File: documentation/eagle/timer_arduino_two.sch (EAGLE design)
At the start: 25 parts, among them J1 SMA420564 LED module, Q1 16 Mhz, U1 328P, U2 LM317

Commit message: Version 1.0
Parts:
- removed J1: SMA420564 LED module, SparkFun-Connectors:CONN_12
- removed R5: 200, eagle-ltspice:R
- added LED1: SMA420564, hp-displays:5082-7414
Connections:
- removed net A: J1.11, R16.2
- removed net B: J1.7, R11.2
- removed net C: J1.4, R10.2
- removed net D: J1.2, R9.2
- removed net D1: J1.12, U1.PB5(SCK)
- removed net D4: J1.6, U1.PB2(SS/OC1B)
- removed net DP: J1.3, R5.2
- removed net E: J1.1, R8.2
- removed net F: J1.10, R7.2
- removed net G: J1.5, R6.2
- removed net N$23: R5.1, U1.PB1(OC1A)
- new net N$14: LED1.C1, U1.PB5(SCK)
- new net N$15: LED1.C4, U1.PB2(SS/OC1B)
- new net N$16: LED1.A, R16.2
- new net N$24: LED1.B
- new net N$28: LED1.C
- new net N$29: LED1.D
- new net N$30: R7.2
- new net N$31: R6.2
- new net N$32: LED1.G
- new net N$33: LED1.F
- new net N$34: LED1.E
- net D2: now also LED1.C2; no longer J1.9
- net D3: now also LED1.C3; no longer J1.8

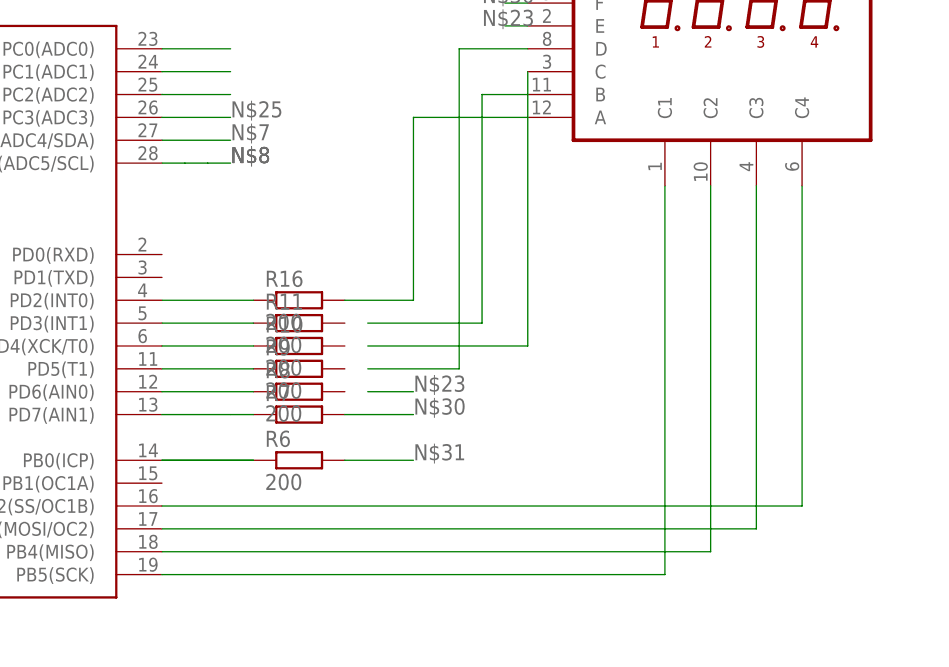
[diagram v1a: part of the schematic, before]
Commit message: adding transistors to design
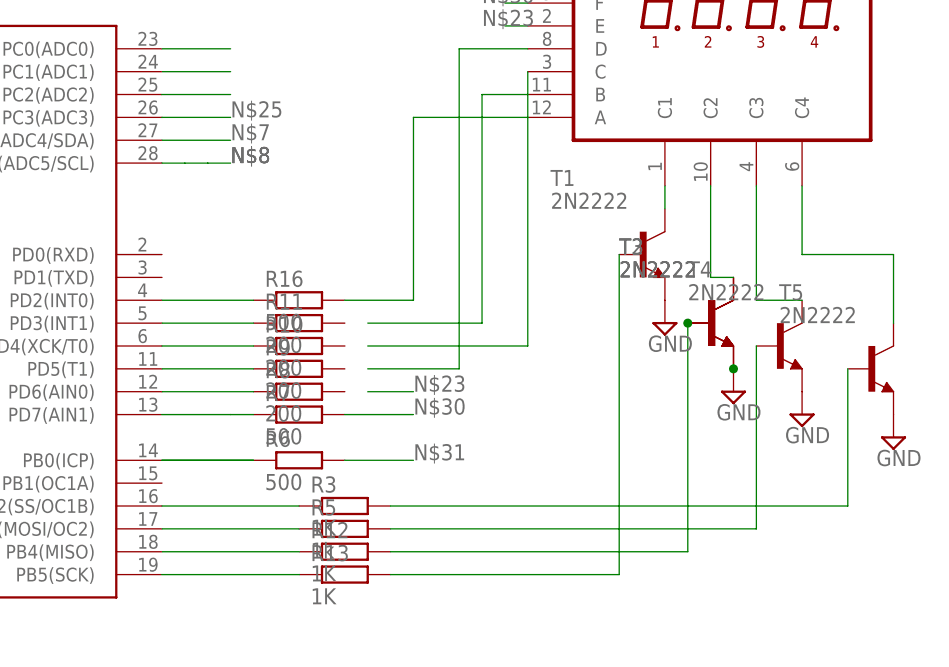
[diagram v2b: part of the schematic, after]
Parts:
- added R12, R13, R3: 1K, eagle-ltspice:R
- added R5: 1k, eagle-ltspice:R
- added T1, T2, T3, T4, T5: 2N2222, transistor:2N2222
- R16, R6: value 200 -> 500
- R7: value (none) -> 500
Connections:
- removed net D2: LED1.C2, U1.PB4(MISO)
- removed net D3: LED1.C3, U1.PB3(MOSI/OC2)
- new net N$35: R5.1, U1.PB3(MOSI/OC2)
- new net N$36: R3.1, U1.PB2(SS/OC1B)
- new net N$37: R12.2, T2.B, T3.B
- new net N$39: LED1.C2, T2.C, T3.C
- new net N$41: LED1.C1, T1.C
- new net N$42: LED1.C3, T4.C
- new net N$43: LED1.C4, T5.C
- new net N$44: R13.2, T1.B
- new net N$45: R5.2, T4.B
- new net N$46: R3.2, T5.B
- net GND: now also T1.E, T2.E, T3.E, T4.E, T5.E
- net N$14: now also R13.1; no longer LED1.C1
- net N$15: now also R12.1, U1.PB4(MISO); no longer LED1.C4, U1.PB2(SS/OC1B)

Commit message: changing eagle library footprint for SM420564
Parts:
- removed LED1: SMA420564, hp-displays:5082-7414
- added SM420564.: NFD-5641AS, display-nfd:NFD-5641AS
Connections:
- removed net N$32: LED1.G
- removed net N$33: LED1.F
- removed net N$34: LED1.E
- new net N$23: R11.2, SM420564..P$7
- net N$16: now also SM420564..P$11; no longer LED1.A
- net N$24: now also R10.2, SM420564..P$4; no longer LED1.B
- net N$28: now also R9.2, SM420564..P$2; no longer LED1.C
- net N$29: now also R8.2, SM420564..P$1; no longer LED1.D
- net N$30: now also SM420564..P$10
- net N$31: now also SM420564..P$5
- net N$39: now also SM420564..P$9; no longer LED1.C2
- net N$41: now also SM420564..P$12; no longer LED1.C1
- net N$42: now also SM420564..P$8; no longer LED1.C3
- net N$43: now also SM420564..P$6; no longer LED1.C4
